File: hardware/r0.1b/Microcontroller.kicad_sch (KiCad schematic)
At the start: 94 parts, among them J10 UART, J2 USB_C, J3 OLED, J8 +12V, J9 STLink, SW1 Button Up, SW2 Button Down, SW3 Reset, SW4 Button Escape, SW5 Button Left, SW6 Button Enter, SW7 Button Right, U10 STM32F405RGTx, U11 TPS5431DDA, U2 LM1117-3.3, U3 USBLC6-2, U4 W25Q16, X1 12 MHz TCXO, Y1 8 MHz

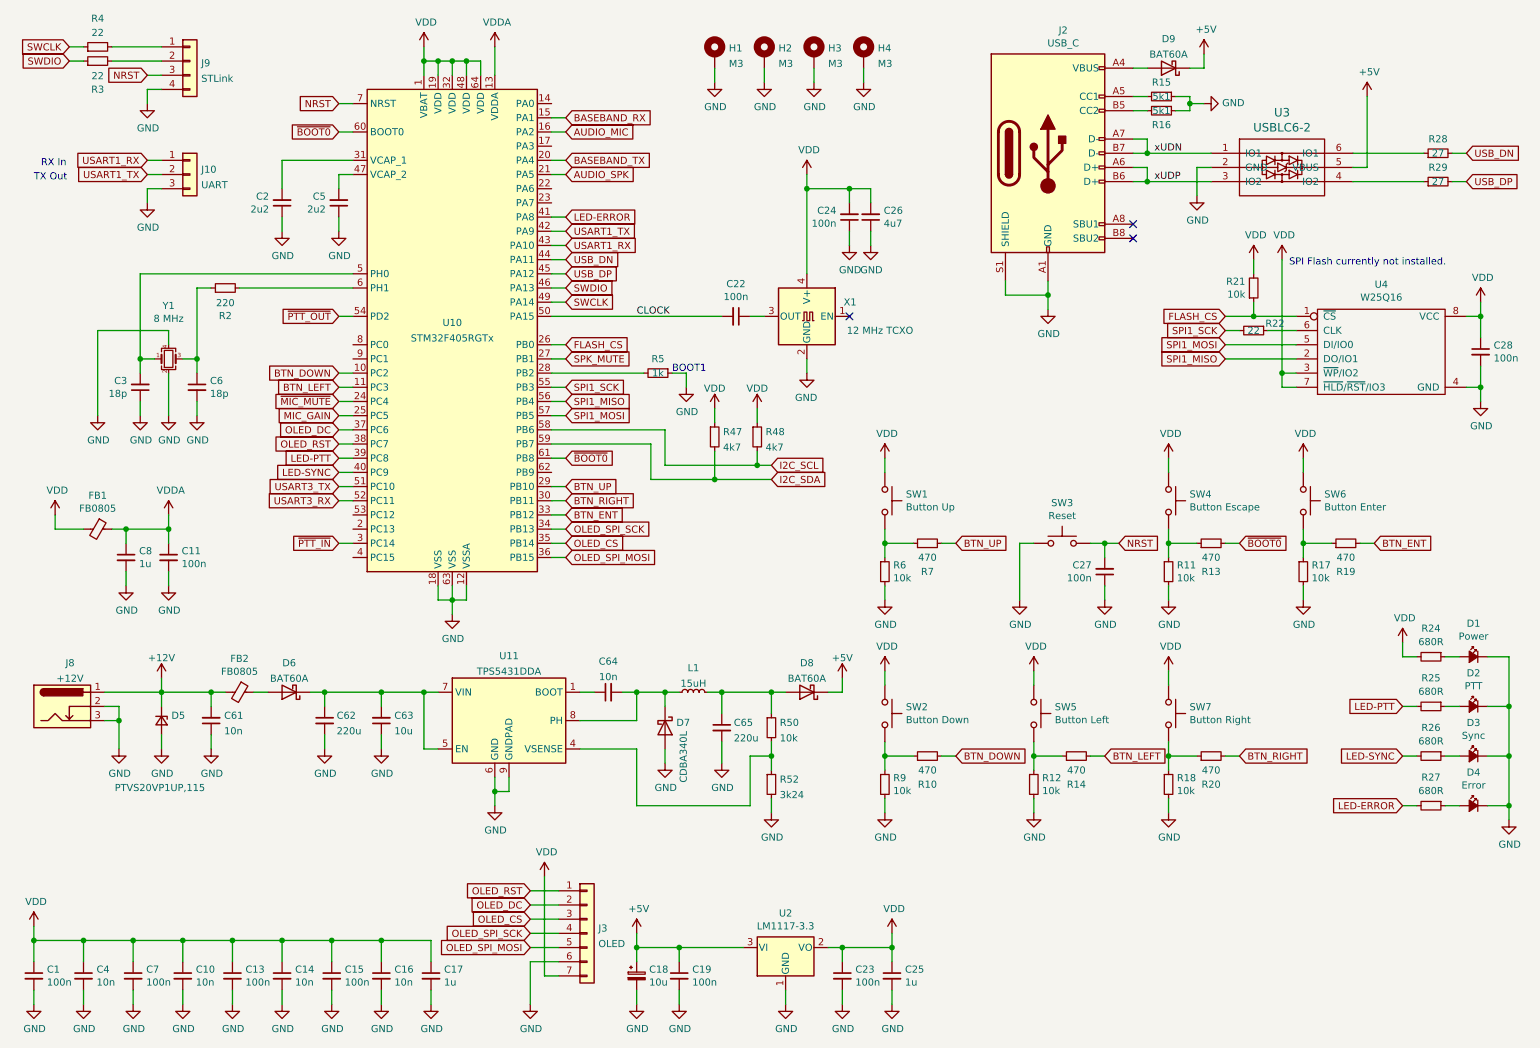
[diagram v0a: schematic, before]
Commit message: Added RTC
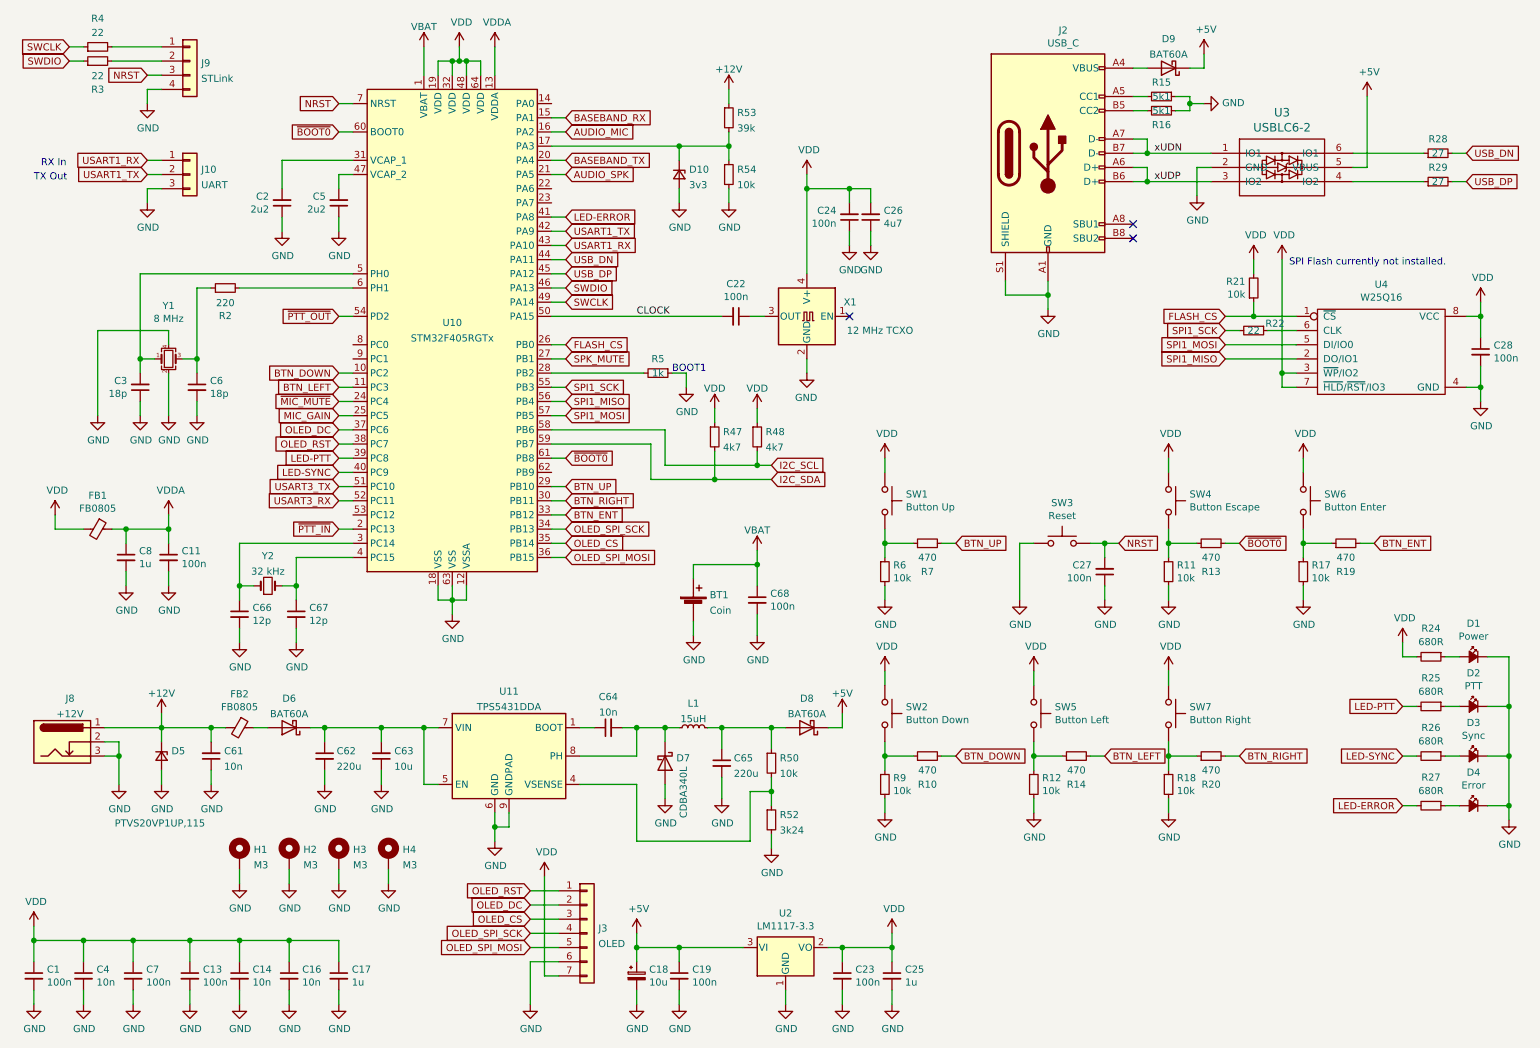
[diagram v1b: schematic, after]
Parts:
- removed C10: 10n, pkl_dipol:C_0603, symbol pkl_device:pkl_C_Small
- removed C15: 100n, pkl_dipol:C_0603, symbol pkl_device:pkl_C_Small
- added BT1: Coin, Battery:BatteryHolder_Keystone_3000_1x12mm, symbol Device:Battery_Cell
- added C66, C67: 12p, pkl_dipol:C_0603, symbol pkl_device:pkl_C_Small
- added C68: 100n, pkl_dipol:C_0603, symbol pkl_device:pkl_C_Small
- added D10: 3v3, Diode_SMD:D_SOD-523, symbol Device:D_Zener_Small
- added R53: 39k, pkl_dipol:R_0603, symbol pkl_device:pkl_R_Small
- added R54: 10k, pkl_dipol:R_0603, symbol pkl_device:pkl_R_Small
- added Y2: 32 kHz, Crystal:Crystal_SMD_MicroCrystal_CC8V-T1A-2Pin_2.0x1.2mm, symbol Device:Crystal_Small
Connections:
- net +12V: now also R53.1
- net GND: now also BT1.2 (-), C66.2, C67.2, C68.2, D10.2 (A), R54.2
- net VDD: no longer U10.1 (VBAT)
- net ~{PTT_IN}: now also U10.2 (PC13); no longer U10.3 (PC14)
- net at U10.17 (PA3): now also D10.1 (K), R53.2, R54.1
- net at U10.4 (PC15): now also C67.1, Y2.2
- new net: C66.1, U10.3 (PC14), Y2.1
- new net VBAT: BT1.1 (+), C68.1, U10.1 (VBAT)
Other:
- moved on the sheet: C13, C14, C16, C17, C61, C62, C63, C64, C65, D5, D6, D7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
